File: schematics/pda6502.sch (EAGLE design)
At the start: 25 parts, among them IC1 74HC00D, IC2 74HC138D, IC3 DS1813-SMD, U1 W65C02S, U2 W65C22S, U3 28C256, U4 UM61256AK-12

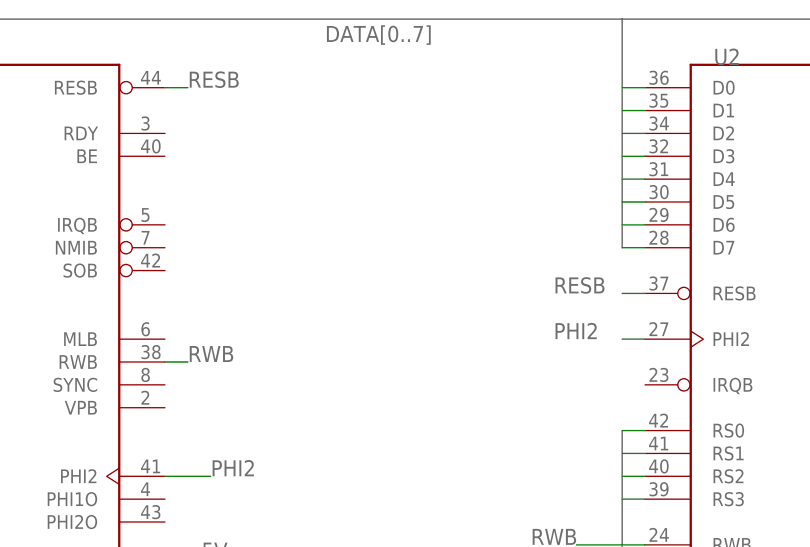
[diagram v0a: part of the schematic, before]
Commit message: schematics: 6502 IRQ to 6522, unused active-low inputs to VCC.
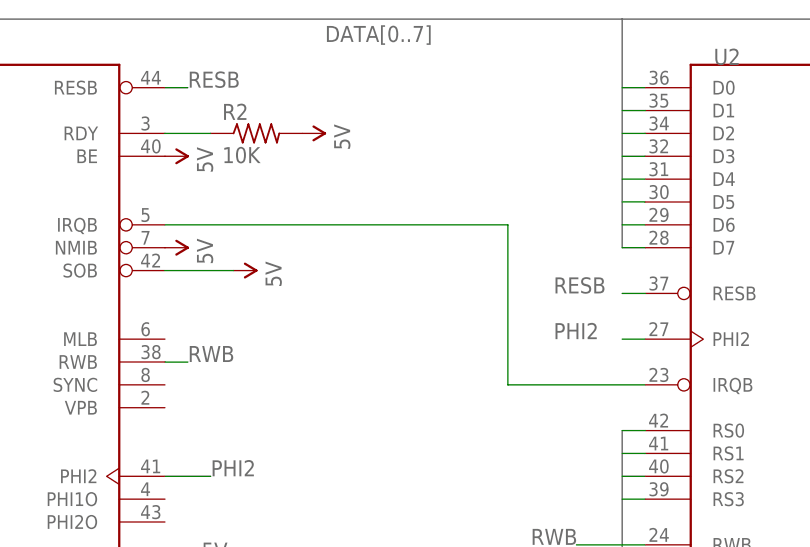
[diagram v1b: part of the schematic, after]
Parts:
- added R2: 10K, resistor:R-US_R0805
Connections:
- new net N$8: U1.IRQB, U2.IRQB
- new net N$9: R2.1, U1.RDY
- net 5V: now also R2.2, U1.BE, U1.NMIB, U1.SOB
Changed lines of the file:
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@@
 <part name="SUPPLY13" library="SparkFun-Aesthetics" deviceset="5V" device=""/>
 <part name="GND16" library="SparkFun-Aesthetics" deviceset="GND" device=""/>
+<part name="SUPPLY14" library="SparkFun-Aesthetics" deviceset="5V" device=""/>
+<part name="SUPPLY15" library="SparkFun-Aesthetics" deviceset="5V" device=""/>
+<part name="SUPPLY16" library="SparkFun-Aesthetics" deviceset="5V" device=""/>
+<part name="R2" library="resistor" deviceset="R-US_" device="R0805" value="10K"/>
+<part name="SUPPLY17" library="SparkFun-Aesthetics" deviceset="5V" device=""/>
 </parts>
 <sheets>
@@
 <instance part="SUPPLY13" gate="G$1" x="165.1" y="121.92"/>
 <instance part="GND16" gate="1" x="154.94" y="116.84"/>
+<instance part="SUPPLY14" gate="G$1" x="45.72" y="147.32" rot="R270"/>
+<instance part="SUPPLY15" gate="G$1" x="38.1" y="149.86" rot="R270"/>
+<instance part="SUPPLY16" gate="G$1" x="38.1" y="160.02" rot="R270"/>
+<instance part="R2" gate="G$1" x="48.26" y="162.56"/>
+<instance part="SUPPLY17" gate="G$1" x="53.34" y="162.56" rot="R270"/>
 </instances>
 <busses>
@@
 <junction x="213.36" y="109.22"/>
 </segment>
+<segment>
+<pinref part="U1" gate="G$1" pin="SOB"/>
+<pinref part="SUPPLY14" gate="G$1" pin="5V"/>
+<wire x1="45.72" y1="147.32" x2="38.1" y2="147.32" width="0.1524" layer="91"/>
+</segment>
+<segment>
+<pinref part="U1" gate="G$1" pin="NMIB"/>
+<pinref part="SUPPLY15" gate="G$1" pin="5V"/>
+</segment>
+<segment>
+<pinref part="U1" gate="G$1" pin="BE"/>
+<pinref part="SUPPLY16" gate="G$1" pin="5V"/>
+</segment>
+<segment>
+<pinref part="R2" gate="G$1" pin="2"/>
+<pinref part="SUPPLY17" gate="G$1" pin="5V"/>
+</segment>
 </net>
 <net name="PA0" class="0">
@@
 </segment>
 </net>
+<net name="N$8" class="0">
+<segment>
+<pinref part="U1" gate="G$1" pin="IRQB"/>
+<wire x1="38.1" y1="152.4" x2="76.2" y2="152.4" width="0.1524" layer="91"/>
+<wire x1="76.2" y1="152.4" x2="76.2" y2="134.62" width="0.1524" layer="91"/>
+<pinref part="U2" gate="G$1" pin="IRQB"/>
+<wire x1="76.2" y1="134.62" x2="91.44" y2="134.62" width="0.1524" layer="91"/>
+</segment>
+</net>
+<net name="N$9" class="0">
+<segment>
+<pinref part="U1" gate="G$1" pin="RDY"/>
+<pinref part="R2" gate="G$1" pin="1"/>
+<wire x1="38.1" y1="162.56" x2="43.18" y2="162.56" width="0.1524" layer="91"/>
+</segment>
+</net>

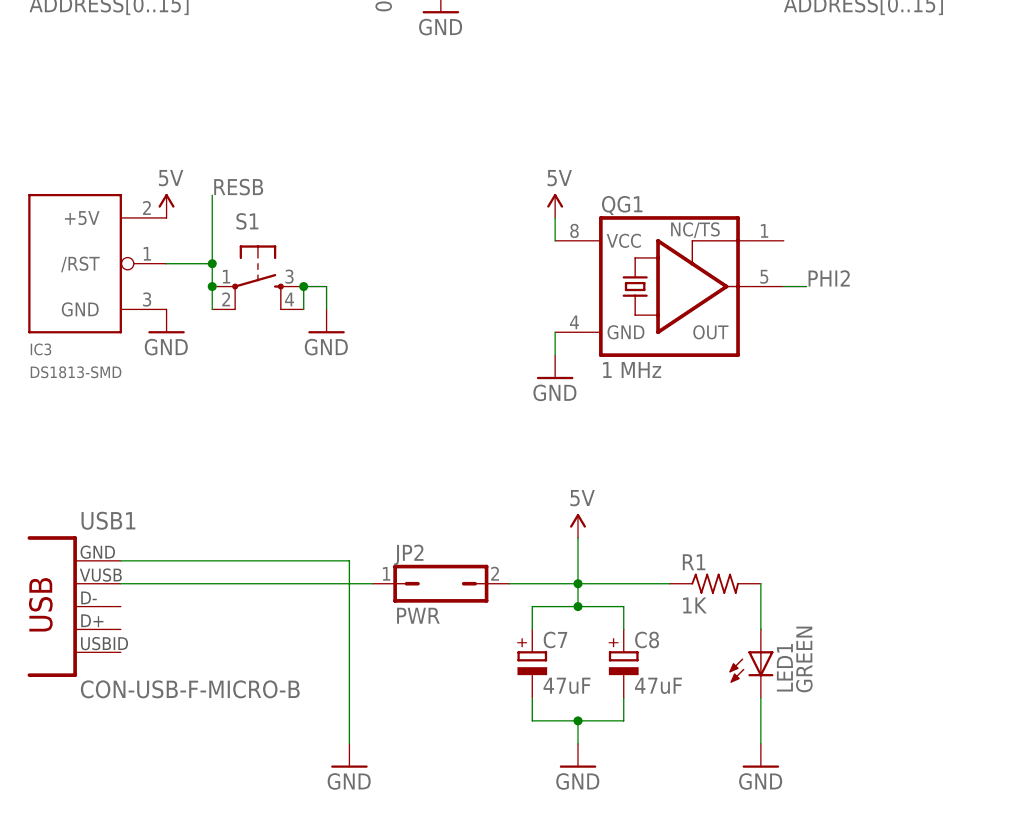
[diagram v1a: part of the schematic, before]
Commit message: schematics: compacted PSU schematic, and clock circuit.
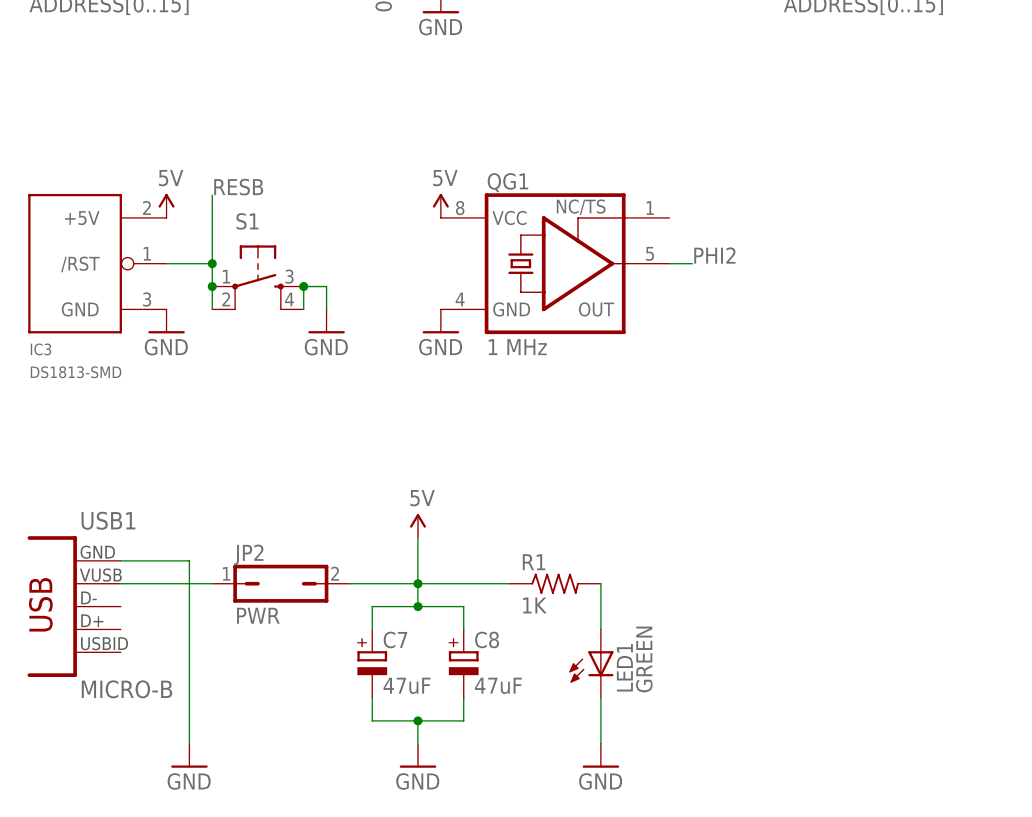
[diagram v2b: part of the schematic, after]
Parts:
- USB1: value CON-USB-F-MICRO-B -> MICRO-B
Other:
- moved on the sheet: C7, C8, JP2, LED1, QG1, R1
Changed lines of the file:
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@@
 <part name="LED1" library="dangerousprototypes_devices" deviceset="LED" device="-0805" value="GREEN"/>
 <part name="GND14" library="SparkFun-Aesthetics" deviceset="GND" device=""/>
-<part name="USB1" library="dangerousprototypes_devices" deviceset="CON-USB-F" device="-MICRO-B"/>
+<part name="USB1" library="dangerousprototypes_devices" deviceset="CON-USB-F" device="-MICRO-B" value="MICRO-B"/>
 <part name="JP2" library="jumper" deviceset="JP1Q" device="" value="PWR"/>
 <part name="GND3" library="SparkFun-Aesthetics" deviceset="GND" device=""/>
@@
 <instance part="SUPPLY9" gate="G$1" x="20.32" y="68.58"/>
 <instance part="GND10" gate="1" x="20.32" y="55.88"/>
-<instance part="QG1" gate="G$1" x="76.2" y="60.96"/>
-<instance part="SUPPLY7" gate="G$1" x="63.5" y="68.58"/>
-<instance part="GND7" gate="1" x="63.5" y="50.8"/>
+<instance part="QG1" gate="G$1" x="63.5" y="63.5"/>
+<instance part="SUPPLY7" gate="G$1" x="50.8" y="68.58"/>
+<instance part="GND7" gate="1" x="50.8" y="55.88"/>
 <instance part="S1" gate="S" x="30.48" y="60.96"/>
 <instance part="GND13" gate="1" x="38.1" y="55.88"/>
@@
 <instance part="C2" gate="G$1" x="48.26" y="99.06" rot="R270"/>
 <instance part="C1" gate="G$1" x="48.26" y="109.22" rot="R270"/>
-<instance part="GND9" gate="1" x="40.64" y="7.62"/>
-<instance part="C7" gate="C" x="60.96" y="20.32"/>
-<instance part="C8" gate="C" x="71.12" y="20.32"/>
-<instance part="R1" gate="G$1" x="81.28" y="27.94"/>
-<instance part="SUPPLY10" gate="G$1" x="66.04" y="33.02"/>
-<instance part="GND11" gate="1" x="66.04" y="7.62"/>
-<instance part="LED1" gate="LED" x="86.36" y="20.32"/>
-<instance part="GND14" gate="1" x="86.36" y="7.62"/>
+<instance part="GND9" gate="1" x="22.86" y="7.62"/>
+<instance part="C7" gate="C" x="43.18" y="20.32"/>
+<instance part="C8" gate="C" x="53.34" y="20.32"/>
+<instance part="R1" gate="G$1" x="63.5" y="27.94"/>
+<instance part="SUPPLY10" gate="G$1" x="48.26" y="33.02"/>
+<instance part="GND11" gate="1" x="48.26" y="7.62"/>
+<instance part="LED1" gate="LED" x="68.58" y="20.32"/>
+<instance part="GND14" gate="1" x="68.58" y="7.62"/>
 <instance part="USB1" gate="USB" x="10.16" y="25.4"/>
-<instance part="JP2" gate="A" x="50.8" y="27.94" rot="R270"/>
+<instance part="JP2" gate="A" x="33.02" y="27.94" rot="R270"/>
 <instance part="GND3" gate="1" x="50.8" y="91.44"/>
 <instance part="IC1" gate="A" x="193.04" y="63.5"/>
@@
 </segment>
 <segment>
-<pinref part="QG1" gate="G$1" pin="GND"/>
-<pinref part="GND7" gate="1" pin="GND"/>
-<wire x1="63.5" y1="55.88" x2="63.5" y2="53.34" width="0.1524" layer="91"/>
-</segment>
-<segment>
 <pinref part="GND9" gate="1" pin="GND"/>
-<wire x1="40.64" y1="30.48" x2="40.64" y2="10.16" width="0.1524" layer="91"/>
+<wire x1="22.86" y1="30.48" x2="22.86" y2="10.16" width="0.1524" layer="91"/>
 <pinref part="USB1" gate="USB" pin="GND"/>
-<wire x1="40.64" y1="30.48" x2="15.24" y2="30.48" width="0.1524" layer="91"/>
+<wire x1="22.86" y1="30.48" x2="15.24" y2="30.48" width="0.1524" layer="91"/>
 </segment>
 <segment>
 <pinref part="C7" gate="C" pin="-"/>
-<wire x1="60.96" y1="15.24" x2="60.96" y2="12.7" width="0.1524" layer="91"/>
-<wire x1="60.96" y1="12.7" x2="66.04" y2="12.7" width="0.1524" layer="91"/>
+<wire x1="43.18" y1="15.24" x2="43.18" y2="12.7" width="0.1524" layer="91"/>
+<wire x1="43.18" y1="12.7" x2="48.26" y2="12.7" width="0.1524" layer="91"/>
 <pinref part="C8" gate="C" pin="-"/>
-<wire x1="66.04" y1="12.7" x2="71.12" y2="12.7" width="0.1524" layer="91"/>
-<wire x1="71.12" y1="12.7" x2="71.12" y2="15.24" width="0.1524" layer="91"/>
+<wire x1="48.26" y1="12.7" x2="53.34" y2="12.7" width="0.1524" layer="91"/>
+<wire x1="53.34" y1="12.7" x2="53.34" y2="15.24" width="0.1524" layer="91"/>
 <pinref part="GND11" gate="1" pin="GND"/>
-<wire x1="66.04" y1="10.16" x2="66.04" y2="12.7" width="0.1524" layer="91"/>
-<junction x="66.04" y="12.7"/>
+<wire x1="48.26" y1="10.16" x2="48.26" y2="12.7" width="0.1524" layer="91"/>
+<junction x="48.26" y="12.7"/>
 </segment>
 <segment>
 <pinref part="LED1" gate="LED" pin="C"/>
 <pinref part="GND14" gate="1" pin="GND"/>
-<wire x1="86.36" y1="15.24" x2="86.36" y2="10.16" width="0.1524" layer="91"/>
+<wire x1="68.58" y1="15.24" x2="68.58" y2="10.16" width="0.1524" layer="91"/>
 </segment>
 <segment>
@@
 <wire x1="154.94" y1="119.38" x2="157.48" y2="119.38" width="0.1524" layer="91"/>
 </segment>
+<segment>
+<pinref part="QG1" gate="G$1" pin="GND"/>
+<pinref part="GND7" gate="1" pin="GND"/>
+</segment>
 </net>
 <net name="5V" class="0">
@@
 </segment>
 <segment>
-<pinref part="QG1" gate="G$1" pin="VCC"/>
-<pinref part="SUPPLY7" gate="G$1" pin="5V"/>
-<wire x1="63.5" y1="68.58" x2="63.5" y2="66.04" width="0.1524" layer="91"/>
-</segment>
-<segment>
 <pinref part="U2" gate="G$1" pin="CS1"/>
 <pinref part="SUPPLY2" gate="G$1" pin="5V"/>
@@
 </segment>
 <segment>
-<wire x1="58.42" y1="27.94" x2="66.04" y2="27.94" width="0.1524" layer="91"/>
-<wire x1="66.04" y1="27.94" x2="66.04" y2="25.4" width="0.1524" layer="91"/>
+<wire x1="40.64" y1="27.94" x2="48.26" y2="27.94" width="0.1524" layer="91"/>
+<wire x1="48.26" y1="27.94" x2="48.26" y2="25.4" width="0.1524" layer="91"/>
 <pinref part="C7" gate="C" pin="+"/>
-<wire x1="60.96" y1="22.86" x2="60.96" y2="25.4" width="0.1524" layer="91"/>
-<wire x1="60.96" y1="25.4" x2="66.04" y2="25.4" width="0.1524" layer="91"/>
-<wire x1="66.04" y1="25.4" x2="71.12" y2="25.4" width="0.1524" layer="91"/>
-<junction x="66.04" y="25.4"/>
+<wire x1="43.18" y1="22.86" x2="43.18" y2="25.4" width="0.1524" layer="91"/>
+<wire x1="43.18" y1="25.4" x2="48.26" y2="25.4" width="0.1524" layer="91"/>
+<wire x1="48.26" y1="25.4" x2="53.34" y2="25.4" width="0.1524" layer="91"/>
+<junction x="48.26" y="25.4"/>
 <pinref part="C8" gate="C" pin="+"/>
-<wire x1="71.12" y1="25.4" x2="71.12" y2="22.86" width="0.1524" layer="91"/>
-<wire x1="66.04" y1="27.94" x2="66.04" y2="33.02" width="0.1524" layer="91"/>
-<junction x="66.04" y="27.94"/>
+<wire x1="53.34" y1="25.4" x2="53.34" y2="22.86" width="0.1524" layer="91"/>
+<wire x1="48.26" y1="27.94" x2="48.26" y2="33.02" width="0.1524" layer="91"/>
+<junction x="48.26" y="27.94"/>
 <pinref part="SUPPLY10" gate="G$1" pin="5V"/>
 <pinref part="R1" gate="G$1" pin="1"/>
-<wire x1="66.04" y1="27.94" x2="76.2" y2="27.94" width="0.1524" layer="91"/>
+<wire x1="48.26" y1="27.94" x2="58.42" y2="27.94" width="0.1524" layer="91"/>
 <pinref part="JP2" gate="A" pin="2"/>
 </segment>
@@
 <pinref part="R2" gate="G$1" pin="2"/>
 <pinref part="SUPPLY17" gate="G$1" pin="5V"/>
+</segment>
+<segment>
+<pinref part="QG1" gate="G$1" pin="VCC"/>
+<pinref part="SUPPLY7" gate="G$1" pin="5V"/>
 </segment>
 </net>
@@
 <segment>
 <pinref part="QG1" gate="G$1" pin="OUT"/>
-<wire x1="88.9" y1="60.96" x2="91.44" y2="60.96" width="0.1524" layer="91"/>
-<label x="91.44" y="60.96" size="1.778" layer="95"/>
+<wire x1="76.2" y1="63.5" x2="78.74" y2="63.5" width="0.1524" layer="91"/>
+<label x="78.74" y="63.5" size="1.778" layer="95"/>
 </segment>
 <segment>
@@
 <pinref part="R1" gate="G$1" pin="2"/>
 <pinref part="LED1" gate="LED" pin="A"/>
-<wire x1="86.36" y1="27.94" x2="86.36" y2="22.86" width="0.1524" layer="91"/>
+<wire x1="68.58" y1="27.94" x2="68.58" y2="22.86" width="0.1524" layer="91"/>
 </segment>
 </net>
@@
 <pinref part="USB1" gate="USB" pin="VUSB"/>
 <pinref part="JP2" gate="A" pin="1"/>
-<wire x1="15.24" y1="27.94" x2="43.18" y2="27.94" width="0.1524" layer="91"/>
-</segment>
-</net>
+<wire x1="15.24" y1="27.94" x2="25.4" y2="27.94" width="0.1524" layer="91"/>
+</segment>
+</net>
